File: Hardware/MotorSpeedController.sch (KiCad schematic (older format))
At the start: 19 parts, among them J1 Conn_01x08_Female, J2 Conn_01x04_Female, U1 ATmega328P-AU, U2 AS5134, Y1 16MHz

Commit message: Updated Footprints for better fit
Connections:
- no-connect marks 0 -> 27
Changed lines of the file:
@@
 Text Notes 8125 4375 0    100  ~ 0
 Motor Encoder
+NoConn ~ 2750 2950
+NoConn ~ 2750 3050
+NoConn ~ 2750 3150
+NoConn ~ 2750 3250
+NoConn ~ 2750 3350
+NoConn ~ 2750 3650
+NoConn ~ 2750 3750
+NoConn ~ 2750 4050
+NoConn ~ 2750 4150
+NoConn ~ 1550 1950
+NoConn ~ 1550 2150
+NoConn ~ 1550 2250
+NoConn ~ 8850 2525
+NoConn ~ 8850 2625
+NoConn ~ 8850 2725
+NoConn ~ 8850 2825
+NoConn ~ 8850 2925
+NoConn ~ 8850 3025
+NoConn ~ 8050 2875
+NoConn ~ 8050 2975
+NoConn ~ 8050 3075
+NoConn ~ 8850 3525
+NoConn ~ 8850 3425
+NoConn ~ 8850 3325
+NoConn ~ 8850 3225
+NoConn ~ 8850 3125
+NoConn ~ 2750 4250
+$Comp
+L power:PWR_FLAG #FLG0101
+U 1 1 600FF68A
+P 875 7050
+F 0 "#FLG0101" H 875 7125 50  0001 C CNN
+F 1 "PWR_FLAG" H 875 7223 50  0000 C CNN
+F 2 "" H 875 7050 50  0001 C CNN
+F 3 "~" H 875 7050 50  0001 C CNN
+	1    875  7050
+	1    0    0    -1
+$EndComp
+$Comp
+L power:PWR_FLAG #FLG0102
+U 1 1 6010216C
+P 1250 7050
+F 0 "#FLG0102" H 1250 7125 50  0001 C CNN
+F 1 "PWR_FLAG" H 1250 7223 50  0000 C CNN
+F 2 "" H 1250 7050 50  0001 C CNN
+F 3 "~" H 1250 7050 50  0001 C CNN
+	1    1250 7050
+	1    0    0    -1
+$EndComp
+$Comp
+L power:+5V #PWR0105
+U 1 1 60103900
+P 600 6925
+F 0 "#PWR0105" H 600 6775 50  0001 C CNN
+F 1 "+5V" H 615 7098 50  0000 C CNN
+F 2 "" H 600 6925 50  0001 C CNN
+F 3 "" H 600 6925 50  0001 C CNN
+	1    600  6925
+	1    0    0    -1
+$EndComp
+Wire Wire Line
+	600  6925 600  7050
+Wire Wire Line
+	600  7050 875  7050
+$Comp
+L power:GND #PWR0106
+U 1 1 60107BEC
+P 1250 7100
+F 0 "#PWR0106" H 1250 6850 50  0001 C CNN
+F 1 "GND" H 1255 6927 50  0000 C CNN
+F 2 "" H 1250 7100 50  0001 C CNN
+F 3 "" H 1250 7100 50  0001 C CNN
+	1    1250 7100
+	1    0    0    -1
+$EndComp
+Wire Wire Line
+	1250 7050 1250 7100
 $EndSCHEMATC

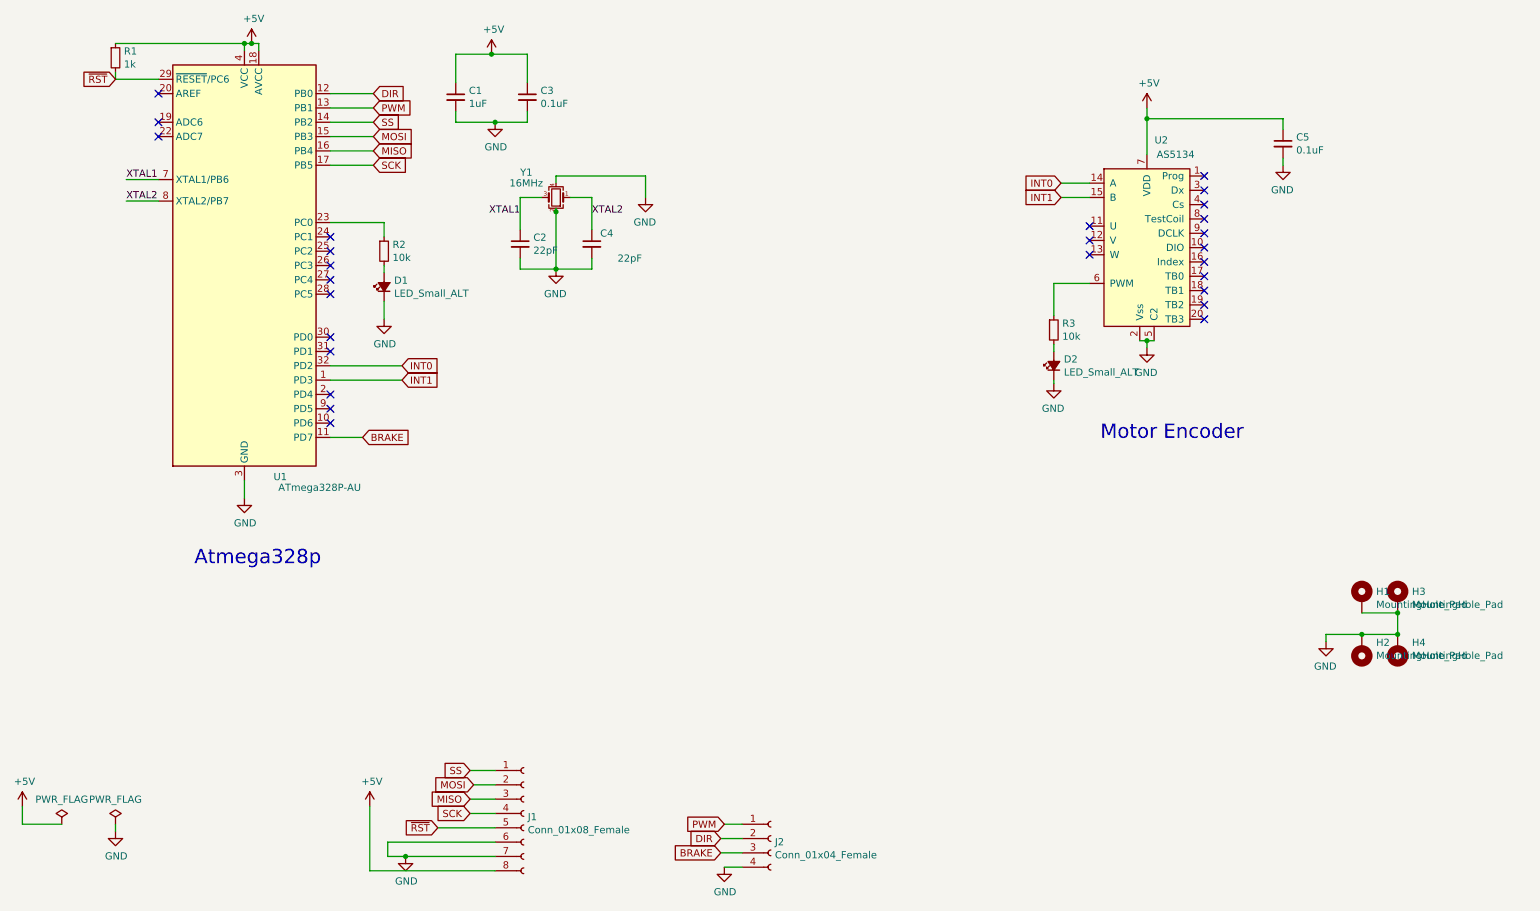
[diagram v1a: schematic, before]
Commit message: Changed PCB Dimensions. Added +5V regulator. Made headers bigger
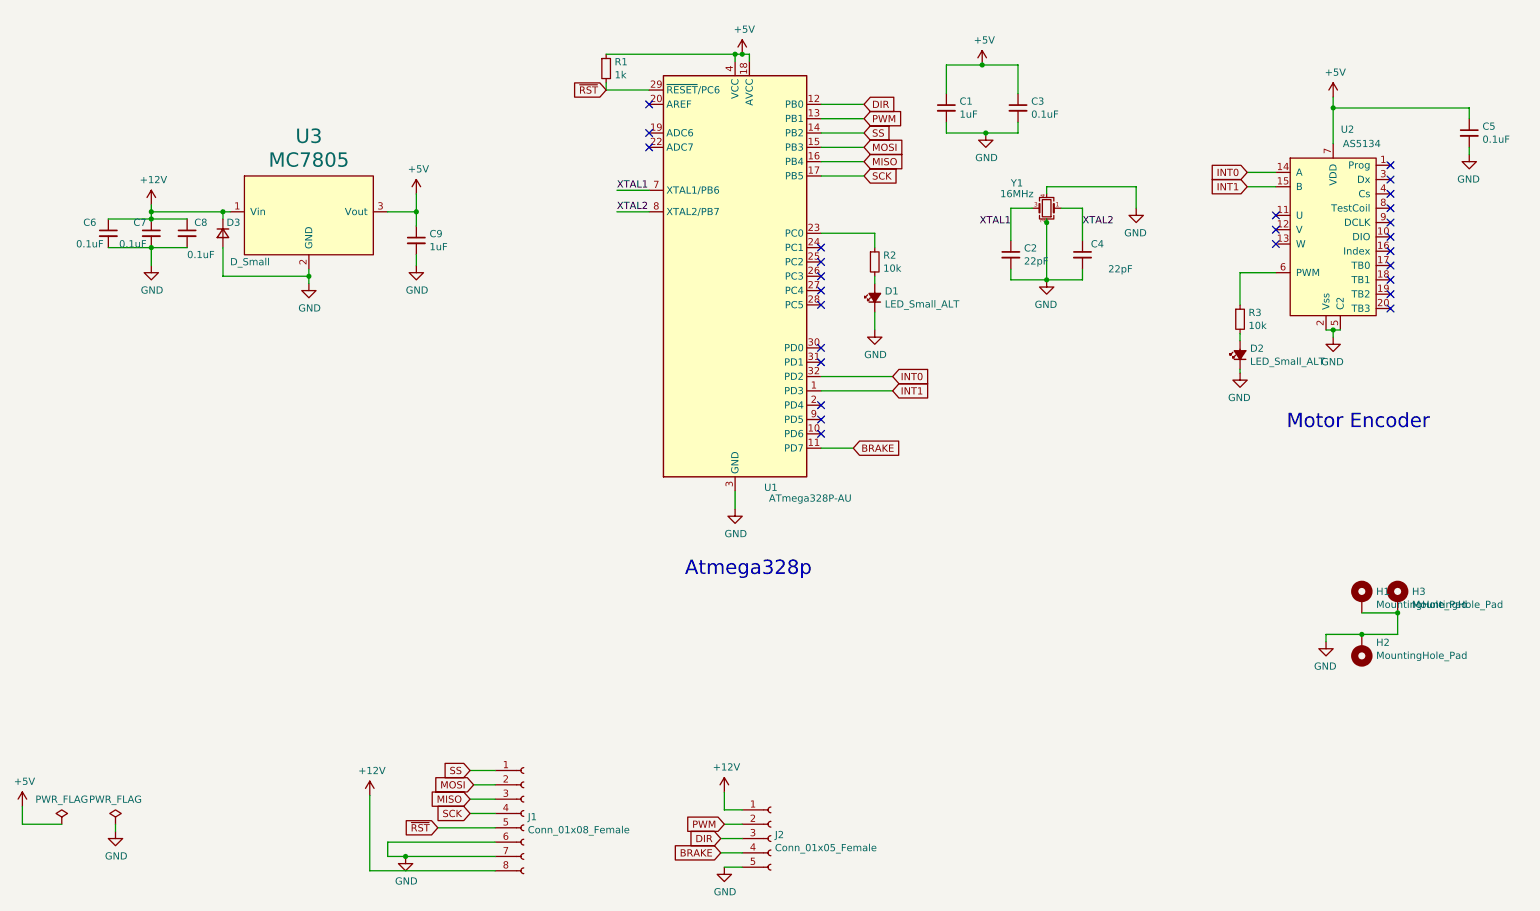
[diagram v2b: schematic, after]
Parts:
- removed H4: MountingHole_Pad, MountingHole:MountingHole_3mm_Pad_Via, symbol Mechanical:MountingHole_Pad
- removed J2: Conn_01x04_Female, Connector_PinHeader_1.27mm:PinHeader_1x04_P1.27mm_Vertical, symbol Connector:Conn_01x04_Female
- added C6, C7, C8: 0.1uF, Capacitor_SMD:C_0603_1608Metric, symbol Device:C_Small
- added C9: 1uF, Capacitor_SMD:C_0603_1608Metric, symbol Device:C_Small
- added D3: D_Small, Diode_SMD:D_2010_5025Metric_Castellated, symbol Device:D_Small
- added J2: Conn_01x05_Female, Connector_PinHeader_2.54mm:PinHeader_1x05_P2.54mm_Vertical, symbol Connector:Conn_01x05_Female
- added U3: MC7805, Package_TO_SOT_SMD:TO-252-2, symbol MotorController:MC7805
- J1: footprint Connector_PinHeader_1.27mm:PinHeader_1x08_P1.27mm_Vertical -> Connector_PinHeader_2.54mm:PinHeader_1x08_P2.54mm_Vertical
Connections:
- net +5V: now also C9.1, U3.3 (Vout); no longer J1.8 (Pin_8)
- net BRAKE: now also J2.4 (Pin_4)
- net DIR: now also J2.3 (Pin_3)
- net GND: now also C6.2, C7.2, C8.2, C9.2, D3.2 (A), J2.5 (Pin_5), U3.2 (GND)
- net PWM: now also J2.2 (Pin_2)
- new net +12V: C6.1, C7.1, C8.1, D3.1 (K), J1.8 (Pin_8), J2.1 (Pin_1), U3.1 (Vin)
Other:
- moved on the sheet: C1, C2, C3, C4, C5, D1, D2, R1, R2, R3, U1, U2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

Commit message: Added Final CAM files and updated BOM
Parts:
- D3: Digikey (none) -> 478-7812-1-ND
- U3: Digikey (none) -> MC7805CDTRKGOSCT-ND
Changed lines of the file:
@@
 F 2 "Package_TO_SOT_SMD:TO-252-2" H 2650 2725 100 0001 C CNN
 F 3 "" H 2600 2775 100 0001 C CNN
+F 4 "MC7805CDTRKGOSCT-ND" H 2600 2775 50  0001 C CNN "Digikey"
 	1    2600 2775
 	1    0    0    -1
@@
 F 2 "Diode_SMD:D_2010_5025Metric_Castellated" V 2000 2925 50  0001 C CNN
 F 3 "~" V 2000 2925 50  0001 C CNN
+F 4 "478-7812-1-ND" V 2000 2925 50  0001 C CNN "Digikey"
 	1    2000 2925
 	0    1    1    0
